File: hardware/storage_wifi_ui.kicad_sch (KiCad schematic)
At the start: 31 parts, among them J16 Keyboard KIN0-7 / KOUT0-7, J17 Keyboard power/reference, J18 I2C0, J19 Full-size SD, SPI, J20 ESP-01S socket, SW2 ESP_PROG, U34 AMS1117-3.3

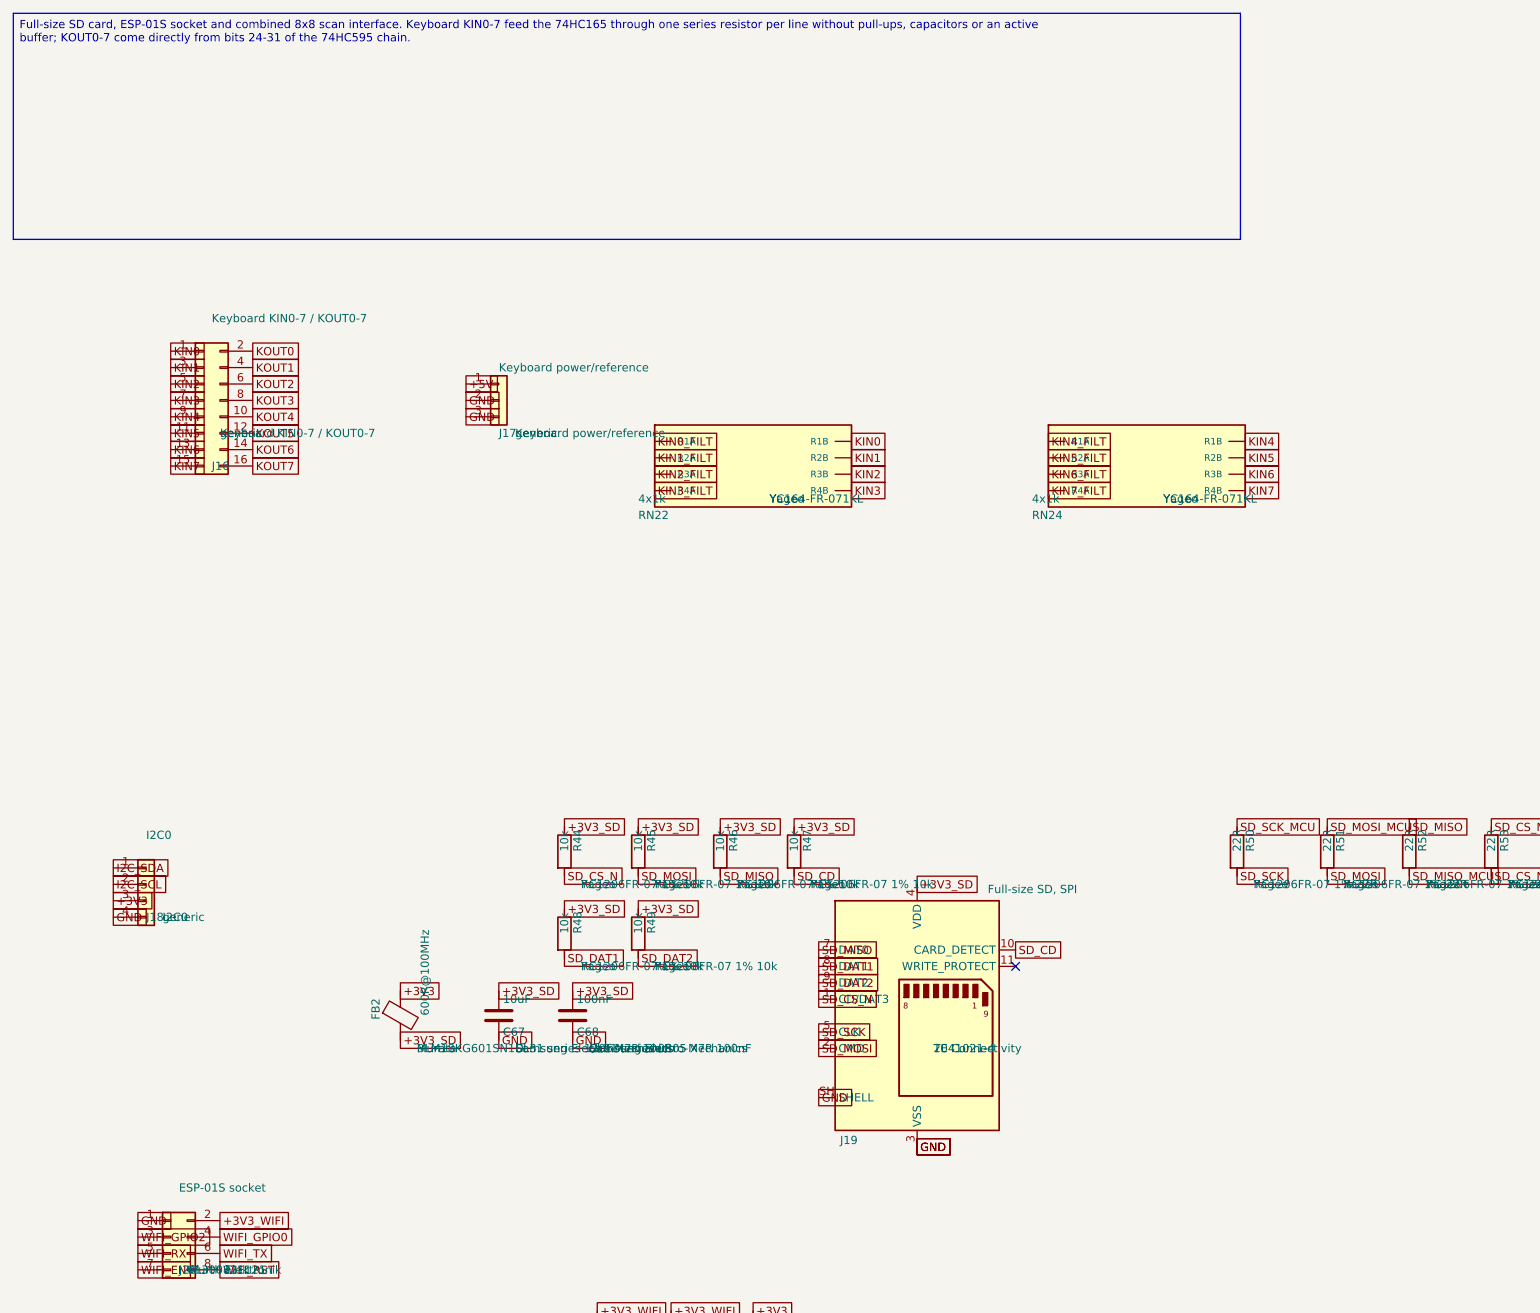
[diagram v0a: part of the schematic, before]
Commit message: Update RP2350B PCB, pinout and fabrication rules
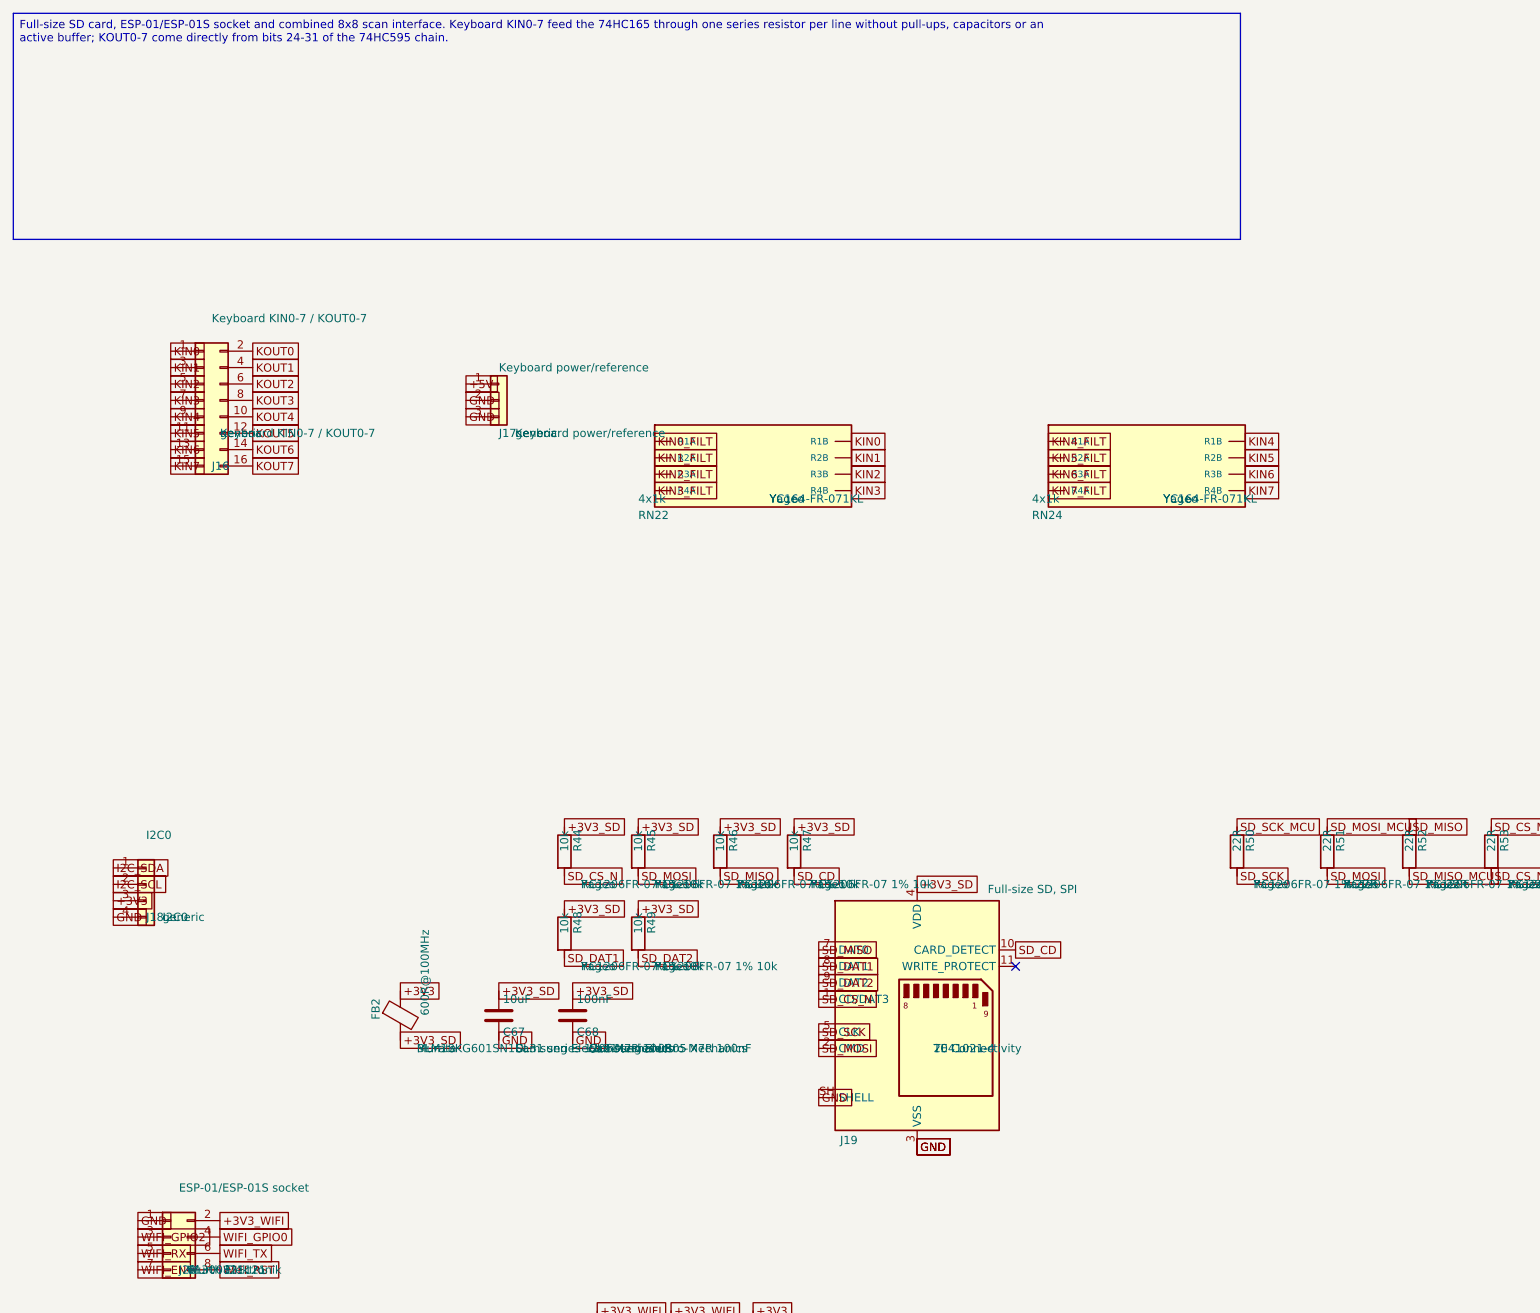
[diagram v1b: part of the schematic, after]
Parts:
- J20: value ESP-01S socket -> ESP-01/ESP-01S socket
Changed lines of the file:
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@@
 		(instances
 			(project "Storage, Wi-Fi and UI"
-				(path "/81a2730e-63ee-4a13-bc2d-cd5138af8d86"
+				(path "/20fbbf79-3608-4116-939f-52752adbdd88"
 					(reference "J16")
 					(unit 1)
@@
 		(instances
 			(project "Storage, Wi-Fi and UI"
-				(path "/81a2730e-63ee-4a13-bc2d-cd5138af8d86"
+				(path "/20fbbf79-3608-4116-939f-52752adbdd88"
 					(reference "J17")
 					(unit 1)
@@
 		(instances
 			(project "Storage, Wi-Fi and UI"
-				(path "/81a2730e-63ee-4a13-bc2d-cd5138af8d86"
+				(path "/20fbbf79-3608-4116-939f-52752adbdd88"
 					(reference "RN22")
 					(unit 1)
@@
 		(instances
 			(project "Storage, Wi-Fi and UI"
-				(path "/81a2730e-63ee-4a13-bc2d-cd5138af8d86"
+				(path "/20fbbf79-3608-4116-939f-52752adbdd88"
 					(reference "RN24")
 					(unit 1)
@@
 		(instances
 			(project "Storage, Wi-Fi and UI"
-				(path "/81a2730e-63ee-4a13-bc2d-cd5138af8d86"
+				(path "/20fbbf79-3608-4116-939f-52752adbdd88"
 					(reference "J18")
 					(unit 1)
@@
 		(instances
 			(project "Storage, Wi-Fi and UI"
-				(path "/81a2730e-63ee-4a13-bc2d-cd5138af8d86"
+				(path "/20fbbf79-3608-4116-939f-52752adbdd88"
 					(reference "J19")
 					(unit 1)
@@
 		(instances
 			(project "Storage, Wi-Fi and UI"
-				(path "/81a2730e-63ee-4a13-bc2d-cd5138af8d86"
+				(path "/20fbbf79-3608-4116-939f-52752adbdd88"
 					(reference "R44")
 					(unit 1)
@@
 		(instances
 			(project "Storage, Wi-Fi and UI"
-				(path "/81a2730e-63ee-4a13-bc2d-cd5138af8d86"
+				(path "/20fbbf79-3608-4116-939f-52752adbdd88"
 					(reference "R45")
 					(unit 1)
@@
 		(instances
 			(project "Storage, Wi-Fi and UI"
-				(path "/81a2730e-63ee-4a13-bc2d-cd5138af8d86"
+				(path "/20fbbf79-3608-4116-939f-52752adbdd88"
 					(reference "R46")
 					(unit 1)
@@
 		(instances
 			(project "Storage, Wi-Fi and UI"
-				(path "/81a2730e-63ee-4a13-bc2d-cd5138af8d86"
+				(path "/20fbbf79-3608-4116-939f-52752adbdd88"
 					(reference "R47")
 					(unit 1)
@@
 		(instances
 			(project "Storage, Wi-Fi and UI"
-				(path "/81a2730e-63ee-4a13-bc2d-cd5138af8d86"
+				(path "/20fbbf79-3608-4116-939f-52752adbdd88"
 					(reference "R48")
 					(unit 1)
@@
 		(instances
 			(project "Storage, Wi-Fi and UI"
-				(path "/81a2730e-63ee-4a13-bc2d-cd5138af8d86"
+				(path "/20fbbf79-3608-4116-939f-52752adbdd88"
 					(reference "R49")
 					(unit 1)
@@
 		(instances
 			(project "Storage, Wi-Fi and UI"
-				(path "/81a2730e-63ee-4a13-bc2d-cd5138af8d86"
+				(path "/20fbbf79-3608-4116-939f-52752adbdd88"
 					(reference "R50")
 					(unit 1)
@@
 		(instances
 			(project "Storage, Wi-Fi and UI"
-				(path "/81a2730e-63ee-4a13-bc2d-cd5138af8d86"
+				(path "/20fbbf79-3608-4116-939f-52752adbdd88"
 					(reference "R51")
 					(unit 1)
@@
 		(instances
 			(project "Storage, Wi-Fi and UI"
-				(path "/81a2730e-63ee-4a13-bc2d-cd5138af8d86"
+				(path "/20fbbf79-3608-4116-939f-52752adbdd88"
 					(reference "R52")
 					(unit 1)
@@
 		(instances
 			(project "Storage, Wi-Fi and UI"
-				(path "/81a2730e-63ee-4a13-bc2d-cd5138af8d86"
+				(path "/20fbbf79-3608-4116-939f-52752adbdd88"
 					(reference "R53")
 					(unit 1)
@@
 		(instances
 			(project "Storage, Wi-Fi and UI"
-				(path "/81a2730e-63ee-4a13-bc2d-cd5138af8d86"
+				(path "/20fbbf79-3608-4116-939f-52752adbdd88"
 					(reference "FB2")
 					(unit 1)
@@
 		(instances
 			(project "Storage, Wi-Fi and UI"
-				(path "/81a2730e-63ee-4a13-bc2d-cd5138af8d86"
+				(path "/20fbbf79-3608-4116-939f-52752adbdd88"
 					(reference "C67")
 					(unit 1)
@@
 		(instances
 			(project "Storage, Wi-Fi and UI"
-				(path "/81a2730e-63ee-4a13-bc2d-cd5138af8d86"
+				(path "/20fbbf79-3608-4116-939f-52752adbdd88"
 					(reference "C68")
 					(unit 1)
@@
 		(instances
 			(project "Storage, Wi-Fi and UI"
-				(path "/81a2730e-63ee-4a13-bc2d-cd5138af8d86"
+				(path "/20fbbf79-3608-4116-939f-52752adbdd88"
 					(reference "R54")
 					(unit 1)
@@
 			)
 		)
-		(property "Value" "ESP-01S socket"
+		(property "Value" "ESP-01/ESP-01S socket"
 			(at 40.64 196.85 0.0000)
 			(effects
@@
 		(instances
 			(project "Storage, Wi-Fi and UI"
-				(path "/81a2730e-63ee-4a13-bc2d-cd5138af8d86"
+				(path "/20fbbf79-3608-4116-939f-52752adbdd88"
 					(reference "J20")
 					(unit 1)
@@
 		(instances
 			(project "Storage, Wi-Fi and UI"
-				(path "/81a2730e-63ee-4a13-bc2d-cd5138af8d86"
+				(path "/20fbbf79-3608-4116-939f-52752adbdd88"
 					(reference "R55")
 					(unit 1)
@@
 		(instances
 			(project "Storage, Wi-Fi and UI"
-				(path "/81a2730e-63ee-4a13-bc2d-cd5138af8d86"
+				(path "/20fbbf79-3608-4116-939f-52752adbdd88"
 					(reference "R56")
 					(unit 1)
@@
 		(instances
 			(project "Storage, Wi-Fi and UI"
-				(path "/81a2730e-63ee-4a13-bc2d-cd5138af8d86"
+				(path "/20fbbf79-3608-4116-939f-52752adbdd88"
 					(reference "R57")
 					(unit 1)
@@
 		(instances
 			(project "Storage, Wi-Fi and UI"
-				(path "/81a2730e-63ee-4a13-bc2d-cd5138af8d86"
+				(path "/20fbbf79-3608-4116-939f-52752adbdd88"
 					(reference "SW2")
 					(unit 1)
@@
 		(instances
 			(project "Storage, Wi-Fi and UI"
-				(path "/81a2730e-63ee-4a13-bc2d-cd5138af8d86"
+				(path "/20fbbf79-3608-4116-939f-52752adbdd88"
 					(reference "C69")
 					(unit 1)
@@
 		(instances
 			(project "Storage, Wi-Fi and UI"
-				(path "/81a2730e-63ee-4a13-bc2d-cd5138af8d86"
+				(path "/20fbbf79-3608-4116-939f-52752adbdd88"
 					(reference "C70")
 					(unit 1)
@@
 		(instances
 			(project "Storage, Wi-Fi and UI"
-				(path "/81a2730e-63ee-4a13-bc2d-cd5138af8d86"
+				(path "/20fbbf79-3608-4116-939f-52752adbdd88"
 					(reference "R58")
 					(unit 1)
@@
 		(instances
 			(project "Storage, Wi-Fi and UI"
-				(path "/81a2730e-63ee-4a13-bc2d-cd5138af8d86"
+				(path "/20fbbf79-3608-4116-939f-52752adbdd88"
 					(reference "U34")
 					(unit 1)
@@
 		(instances
 			(project "Storage, Wi-Fi and UI"
-				(path "/81a2730e-63ee-4a13-bc2d-cd5138af8d86"
+				(path "/20fbbf79-3608-4116-939f-52752adbdd88"
 					(reference "C88")
 					(unit 1)
@@
 		(instances
 			(project "Storage, Wi-Fi and UI"
-				(path "/81a2730e-63ee-4a13-bc2d-cd5138af8d86"
+				(path "/20fbbf79-3608-4116-939f-52752adbdd88"
 					(reference "C89")
 					(unit 1)
@@
 		(at 170.18 162.56)
 	)
-	(text_box "Full-size SD card, ESP-01S socket and combined 8x8 scan interface. Keyboard KIN0-7 feed the 74HC165 through one series resistor per line without pull-ups, capacitors or an active buffer; KOUT0-7 come directly from bits 24-31 of the 74HC595 chain."
+	(text_box "Full-size SD card, ESP-01/ESP-01S socket and combined 8x8 scan interface. Keyboard KIN0-7 feed the 74HC165 through one series resistor per line without pull-ups, capacitors or an active buffer; KOUT0-7 come directly from bits 24-31 of the 74HC595 chain."
 		(exclude_from_sim no)
 		(at 15 15 0.0000)

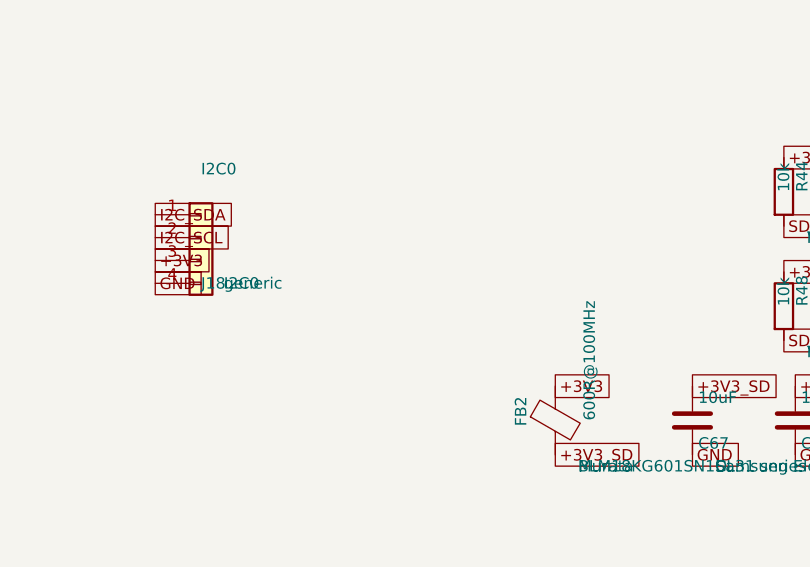
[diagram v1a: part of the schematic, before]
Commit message: Finalize interface routing and repair PCB connectivity
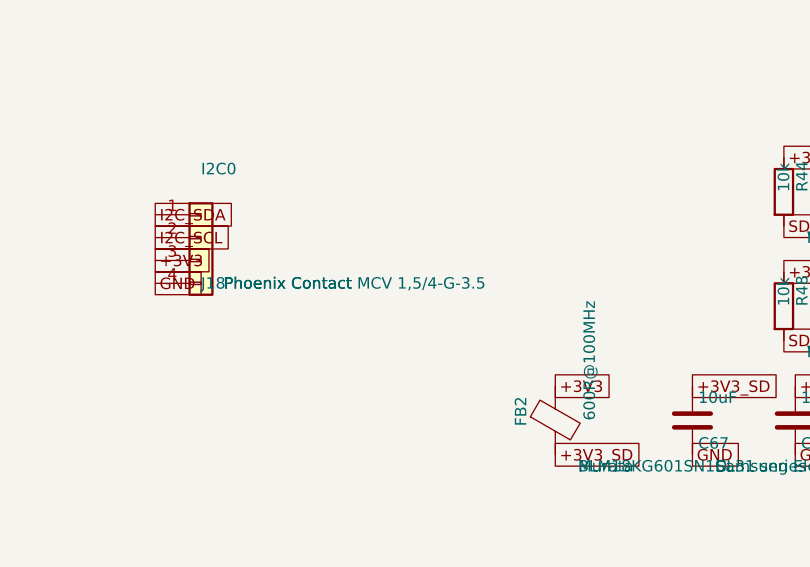
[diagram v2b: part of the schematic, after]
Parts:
- J18: footprint Connector_PinHeader_2.54mm:PinHeader_1x04_P2.54mm_Vertical -> Connector_Phoenix_MC:PhoenixContact_MCV_1,5_4-G-3.5_1x04_P3.50mm_Vertical; MPN I2C0 -> Phoenix Contact MCV 1,5/4-G-3.5; Manufacturer generic -> Phoenix Contact
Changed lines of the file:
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@@
 			)
 		)
-		(property "Footprint" "Connector_PinHeader_2.54mm:PinHeader_1x04_P2.54mm_Vertical"
+		(property "Footprint" "Connector_Phoenix_MC:PhoenixContact_MCV_1,5_4-G-3.5_1x04_P3.50mm_Vertical"
 			(at 35.56 149.86 0.0000)
 			(effects
@@
 			)
 		)
-		(property "MPN" "I2C0"
+		(property "MPN" "Phoenix Contact MCV 1,5/4-G-3.5"
 			(at 38.1 154.9399 0)
 			(effects
@@
 			)
 		)
-		(property "Manufacturer" "generic"
+		(property "Manufacturer" "Phoenix Contact"
 			(at 38.1 154.9399 0)
 			(effects

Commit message: Update RP2350 board power and I/O design
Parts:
- removed R55, R56, R57, R58: 10k, Resistor_SMD:R_1206_3216Metric, symbol Device:R
- added RN36: 4x10k, Resistor_SMD:R_Array_Convex_4x0603, symbol LeanCam:ResistorPack04
- C69, C88: value 10uF -> 22uF 25V; footprint Capacitor_SMD:C_1206_3216Metric -> Capacitor_SMD:C_1210_3225Metric; MPN CL31 series 1206 X7R 10uF -> CL32 series 1210 X7R 22uF 25V
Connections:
- net +3V3_WIFI: now also RN36.1 (R1A), RN36.2 (R2A), RN36.3 (R3A), RN36.4 (R4A)
- net WIFI_EN: now also RN36.8 (R1B)
- net WIFI_GPIO0: now also RN36.6 (R3B)
- net WIFI_GPIO2: now also RN36.5 (R4B)
- net WIFI_RST: now also RN36.7 (R2B)
